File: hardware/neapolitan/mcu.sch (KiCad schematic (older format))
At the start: 134 parts, among them J1 USB-MICRO-B, P1 1V8, P20 GPIO, P22 I2S, P23 DBGEN, P24 TRST, P25 LPC_ISP, P26 LPC_JTAG, P28 SD, P29 CPLD_JTAG, P3 GND, P30 BANK2_AUX, P5 LEDS, P68 SPIFI_CS, P69 VREGMODE, P70 EN_1V8, P71 ID, P72 GP_CLKIN, P73 P1_2, P74 P1_1, P75 GP_CLKIN, P76 GP_CLKIN, P77 GP_CLKIN, P78 GP_CLKIN, P79 GP_CLKIN, P8 VCC, P80 SHIELD, P81 SPIFI_SIO2, P82 SPIFI_SIO3, Q5 MOSFET_P, SW1 DFU, SW2 RESET, U15 LXES1TBCC2-004, U20 W25Q80BV, U21 TPS62410, U23 LPC4320FBD144, U24 GSG-XC2C64A-7VQG100C, X2 MCU_XTAL, X3 RTC_XTAL

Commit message: Neapolitan: deleted MCU and other things not needed
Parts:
- removed C118, C157, C158, C164: 18pF, hackrf:GSG-0402, symbol C
- removed C125: 33pF, hackrf:GSG-0402, symbol C
- removed C126, C127, C143, C145, C146: 10uF, hackrf:GSG-0805, symbol C
- removed C128, C129, C130, C131, C132, C133, C134, C135, C136, C137, C138, C139, C140, C141, C142, C144, C147, C148, C149, C150, C151, C152, C153, C154: 100nF, hackrf:GSG-0402, symbol C
- removed C156: 47pF, hackrf:GSG-0402, symbol C
- removed D4: USBLED, gsg-modules:LTST-S220, symbol LED
- removed D8: 1V8LED, gsg-modules:LTST-S220, symbol LED
- removed L10, L11: 4u7, hackrf:GSG-NRG4026, symbol INDUCTOR
- removed P1: 1V8, hackrf:GSG-HEADER-1x2, symbol CONN_2
- removed P23: DBGEN, hackrf:GSG-TESTPOINT-50MIL, symbol CONN_1
- removed P24: TRST, hackrf:GSG-TESTPOINT-50MIL, symbol CONN_1
- removed P25: LPC_ISP, hackrf:GSG-HEADER-1x6, symbol CONN_6
- removed P26: LPC_JTAG, hackrf:GSG-50MIL-HEADER-2x5-TH, symbol CONN_5X2
- removed P29: CPLD_JTAG, hackrf:GSG-HEADER-1x2, symbol CONN_2
- removed P3: GND, hackrf:GSG-HEADER-NOMARK-1x2, symbol CONN_2
- removed P68: SPIFI_CS, hackrf:GSG-TESTPOINT-50MIL, symbol CONN_1
- removed P69: VREGMODE, hackrf:GSG-TESTPOINT-50MIL, symbol CONN_1
- removed P70: EN_1V8, hackrf:GSG-TESTPOINT-50MIL, symbol CONN_1
- removed P71: ID, hackrf:GSG-TESTPOINT-50MIL, symbol CONN_1
- removed P72, P75, P76, P77, P78, P79: GP_CLKIN, hackrf:GSG-TESTPOINT-50MIL, symbol CONN_1
- removed P73: P1_2, hackrf:GSG-TESTPOINT-50MIL, symbol CONN_1
- removed P74: P1_1, hackrf:GSG-TESTPOINT-50MIL, symbol CONN_1
- removed P8: VCC, hackrf:GSG-HEADER-1x2, symbol CONN_2
- removed P81: SPIFI_SIO2, hackrf:GSG-TESTPOINT-50MIL, symbol CONN_1
- removed P82: SPIFI_SIO3, hackrf:GSG-TESTPOINT-50MIL, symbol CONN_1
- removed Q5: MOSFET_P, gsg-modules:SOT23GDS, symbol MOSFET_P
- removed R100, R19, R30, R34, R77, R78, R79, R80, R81, R86, R87, R88, R89, R90, R91, R96, R98, R99: 39, hackrf:GSG-0402, symbol R
- removed R12, R37, R48, R49, R51, R52, R54, R59, R63, R64, R65, R66, R67, R68, R7, R93: 10k, hackrf:GSG-0402, symbol R
- removed R46, R55: 162k, hackrf:GSG-0402, symbol R
- removed R47: 330k, hackrf:GSG-0402, symbol R
- removed R56: 715k, hackrf:GSG-0402, symbol R
- removed R57, R58, R62: 0, hackrf:GSG-0402, symbol R
- removed R69: 12k, hackrf:GSG-0402, symbol R
- removed R72: 470, hackrf:GSG-0402, symbol R
- removed R76: 1k, hackrf:GSG-0402, symbol R
- removed SW1: DFU, hackrf:GSG-SWITCH-FSMRA, symbol SW_PUSH_SHIELDED
- removed SW2: RESET, hackrf:GSG-SWITCH-FSMRA, symbol SW_PUSH_SHIELDED
- removed U15: LXES1TBCC2-004, hackrf:GSG-LXES1TBCC2-004, symbol LXES1TBCC2-004
- removed U20: W25Q80BV, hackrf:GSG-SOIC8-208, symbol W25Q80BV
- removed U21: TPS62410, hackrf:GSG-S-PVSON-N10, symbol TPS62410
- removed U23: LPC4320FBD144, hackrf:GSG-LQFP144, symbol LPC43XXFBD144
- removed U24: GSG-XC2C64A-7VQG100C, hackrf:GSG-VQ100, symbol GSG-XC2C64A-7VQG100C
- removed X2: MCU_XTAL, hackrf:GSG-XTAL3.2x2.5mm, symbol GSG-XTAL4PIN
- removed X3: RTC_XTAL, hackrf:GSG-XTAL-AB26TRQ, symbol CRYSTAL
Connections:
- net labels removed: 1V8, BANK2F3M1, BANK2F3M10, BANK2F3M11, BANK2F3M14, BANK2F3M15, BANK2F3M16, BANK2F3M3, BANK2F3M5, BANK2F3M7, BANK2F3M8, BANK2F3M9, CPLD_TDO, CPLD_TMS, CS_AD, DA0, DA1, DA2, DA3, DA4, DA5, DA6, DA7, DBGEN, DD0, DD1, DD2, DD3, DD4, DD5, DD6, DD7, DD8, DD9, DM, DP, EN1V8, GP_CLKIN, ISP, MCU_CLK, P1_1, P1_2, REG_OUT1, REG_OUT2, RREF, RTCX1, RTCX2, SGPIO0, SGPIO1, SGPIO10, SGPIO11, SGPIO12, SGPIO13, SGPIO14, SGPIO15, SGPIO2, SGPIO3, SGPIO4, SGPIO5, SGPIO6, SGPIO7, SGPIO8, SGPIO9, SGPIO_CLK, SPIFI_CS, SPIFI_SIO2, SPIFI_SIO3, TCK, TDI, TDO, TMS, VREGMODE, XTAL1, XTAL2
- wire segments 566 -> 152
- no-connect marks 17 -> 3
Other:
- note removed: "1%"
- note removed: "Boot selection:"
- note removed: "Cortex Debug\nConnector\n(10 pin 50 mil)"
- note removed: "Default boot configuration is SPIFI.\nPress SW1 during reset to switch to\nUSB0 (DFU mode)."
- note removed: "GND"
- note removed: "P1_1"
- note removed: "P1_2"
- note removed: "P2_8"
- note removed: "P2_9"
- note removed: "PCB trace jumper"
- note removed: "SPIFI"
- note removed: "SSP0"
- note removed: "Series resistors are here because of a possible\novershoot/undershoot problem. They may be able to be removed\nsafely. Anyway, they probably will minimize damage in the event of\nSGPIO/CPLD misconfiguration."
- note removed: "U23 starts up on this 12 MHz\ncrystal. This makes it possible\nto use USB0 DFU boot mode.\nIt should be possible to switch\nto GP_CLKIN provided by the\nclock generator IC (MCL_CLK)\nif desired."
- note removed: "USART0"
- note removed: "USART3"
- note removed: "USB0"
- note removed: "VCC"

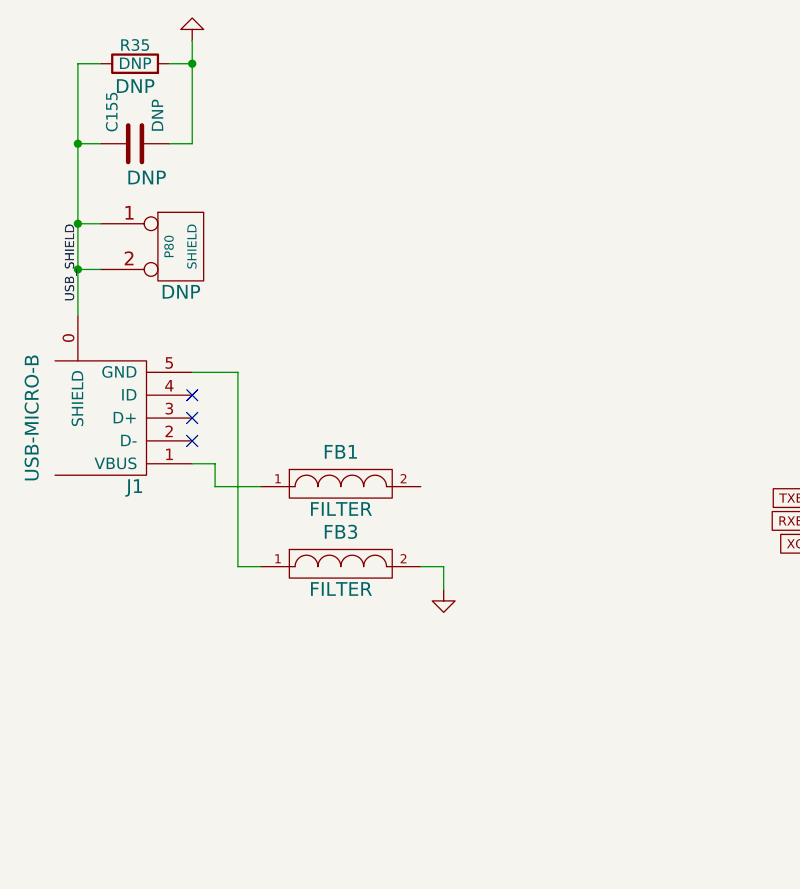
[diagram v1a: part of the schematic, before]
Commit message: Neapolitan: barrel jack and USB power sources that override USB power on main board
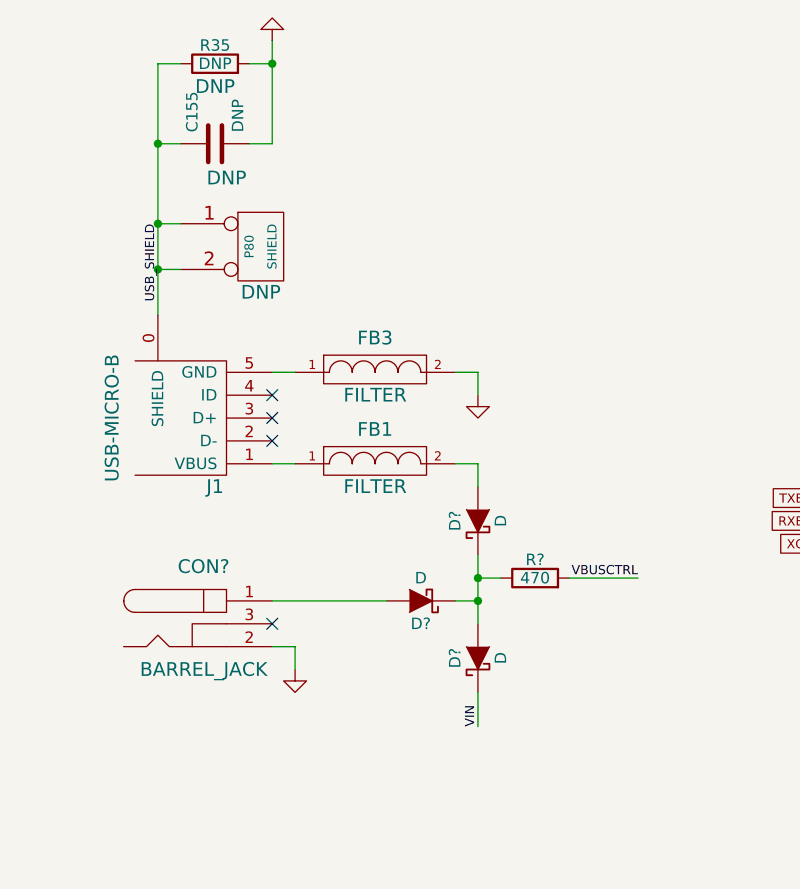
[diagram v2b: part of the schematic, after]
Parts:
- added CON?: BARREL_JACK, symbol BARREL_JACK
- added D? (x3): D, symbol D_Schottky
- added R?: 470, hackrf:GSG-0402, symbol R
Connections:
- wire segments 152 -> 158
- no-connect marks 3 -> 4
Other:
- moved on the sheet: C155, FB1, FB3, J1, P80, R35

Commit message: Neapolitan: header pin assignments
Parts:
- removed P30: BANK2_AUX, hackrf:GSG-HEADER-2x10, symbol CONN_10X2
- D10: renamed from D?; value D -> VIN_DIODE
- D4: renamed from D?; value D -> BARREL_DIODE
- D8: renamed from D?; value D -> VBUS_DIODE
- gave numbers to parts that had none: 2
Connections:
- net labels added: SSP0_MISO, SSP0_MOSI, SSP0_SCK
- net labels removed: B1AUX13, B1AUX14, B2AUX1, B2AUX10, B2AUX11, B2AUX12, B2AUX13, B2AUX14, B2AUX15, B2AUX16, B2AUX2, B2AUX3, B2AUX4, B2AUX5, B2AUX6, B2AUX7, B2AUX8, B2AUX9, BANK2F3M12, BANK2F3M2, BANK2F3M4, BANK2F3M6, CPLD_TCK, CPLD_TDI, GCK0, LED1, SSP1_MISO, SSP1_MOSI, SSP1_SCK
- wire segments 158 -> 116
- no-connect marks 4 -> 13
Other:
- moved on the sheet: D4

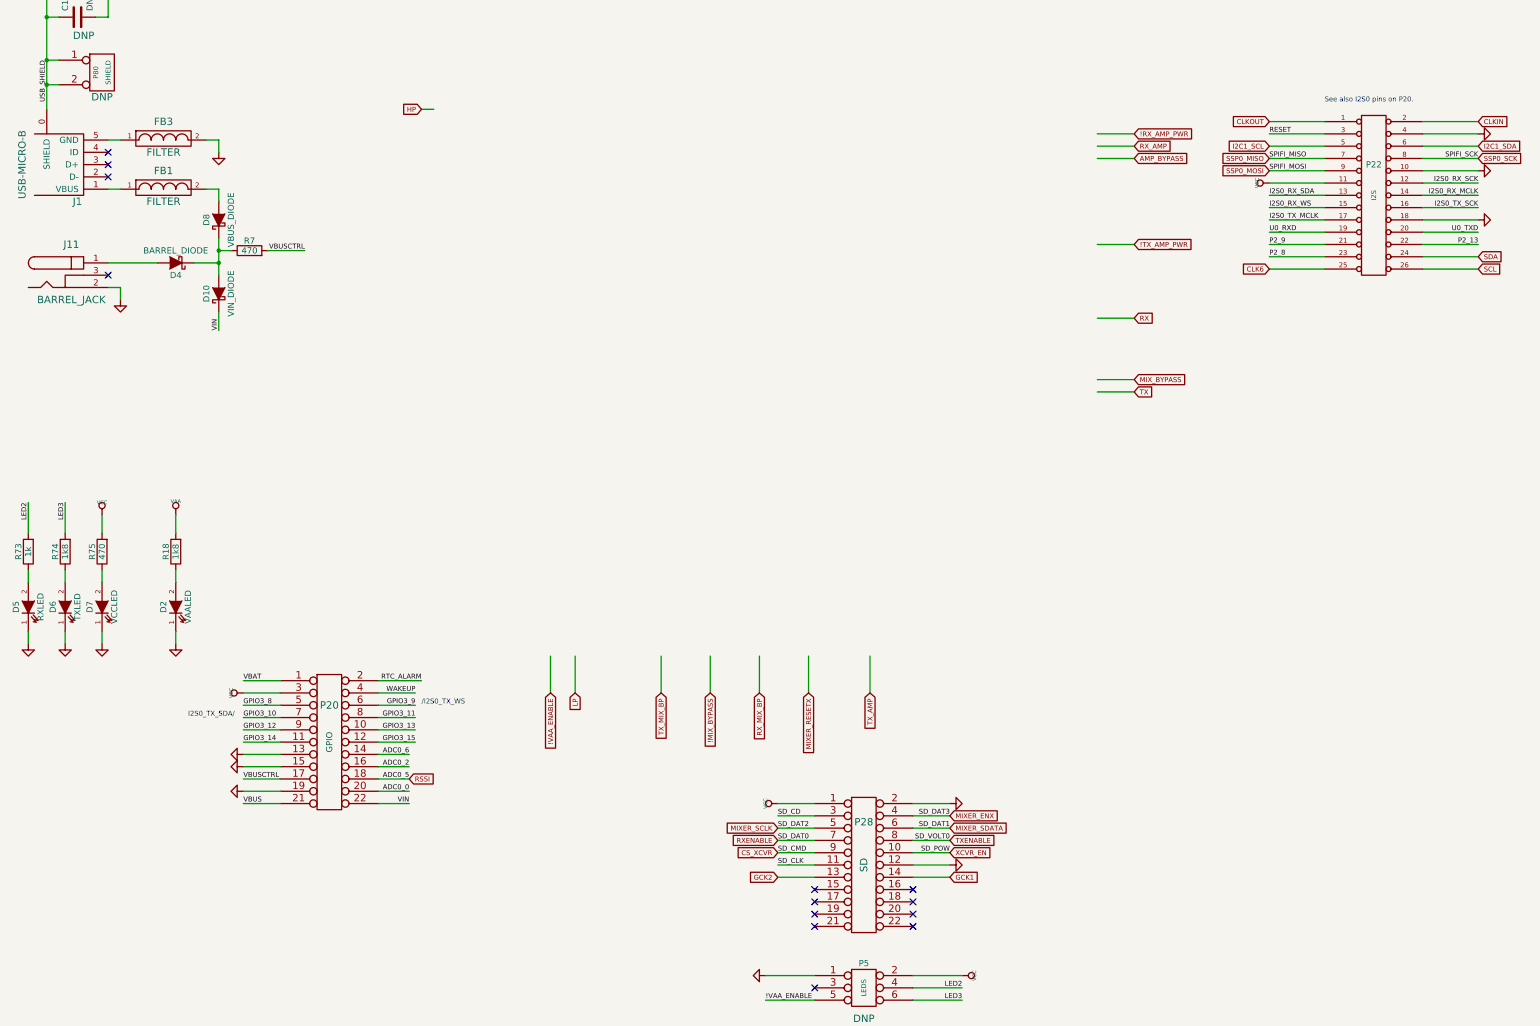
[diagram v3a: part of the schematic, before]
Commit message: Neapolitan: added I/O expander
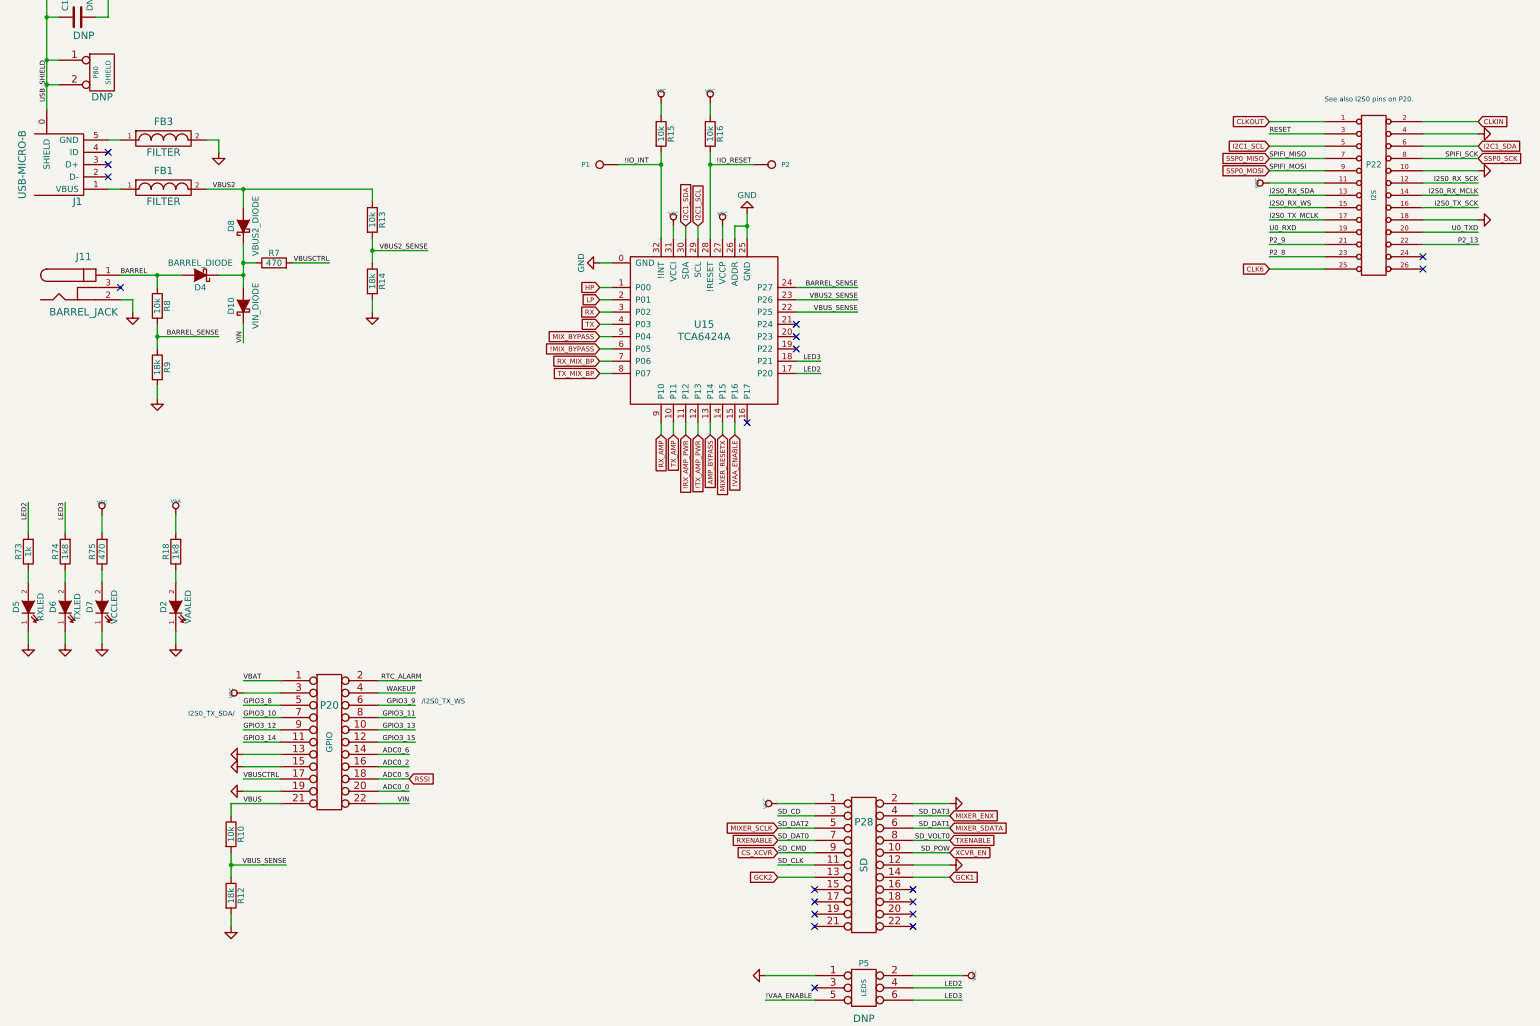
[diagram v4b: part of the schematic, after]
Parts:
- added P1: !IO_INT, hackrf:GSG-TESTPOINT-50MIL, symbol CONN_1
- added P2: !IO_RESET, hackrf:GSG-TESTPOINT-50MIL, symbol CONN_1
- added R10, R13, R15, R16, R8: 10k, hackrf:GSG-0402, symbol R
- added R12, R14, R9: 18k, hackrf:GSG-0402, symbol R
- added U15: TCA6424A, gsg-modules:QFN32-5, symbol TCA6424A
- D10, D4: footprint (none) -> gsg-modules:SOD128
- D8: value VBUS_DIODE -> VBUS2_DIODE; footprint (none) -> gsg-modules:SOD128
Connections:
- net labels added: !IO_INT, !IO_RESET, BARREL, BARREL_SENSE, VBUS2, VBUS2_SENSE, VBUS_SENSE
- net labels removed: SCL, SDA
- wire segments 116 -> 145
- no-connect marks 13 -> 19
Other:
- moved on the sheet: D10, D4, D8, J11, R7

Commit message: Neapolitan: barrel jack module
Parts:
- J11: footprint (none) -> gsg-modules:CUI_PJ-102[AB]H
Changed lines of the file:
@@
 F 0 "J11" H 1450 4700 60  0000 C CNN
 F 1 "BARREL_JACK" H 1450 4250 60  0000 C CNN
-F 2 "" H 1450 4450 60  0001 C CNN
+F 2 "gsg-modules:CUI_PJ-102[AB]H" H 1450 4450 60  0001 C CNN
 F 3 "" H 1450 4450 60  0000 C CNN
 F 4 "CUI" H 1450 4450 60  0001 C CNN "Manufacturer"

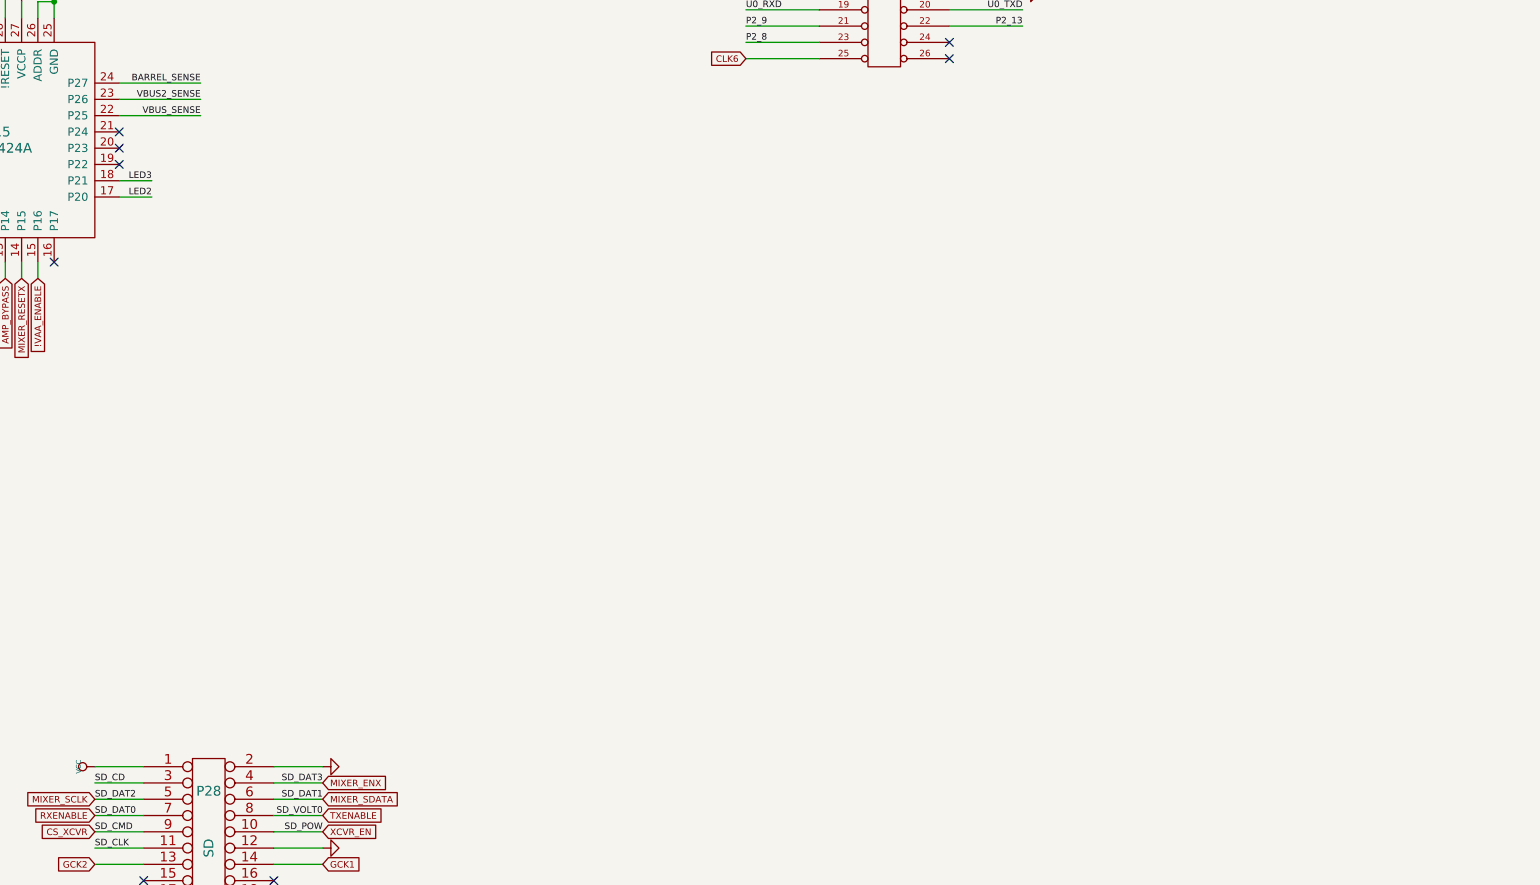
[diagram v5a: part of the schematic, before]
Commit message: Neapolitan: experimental 2.5 ppm clock in schematic
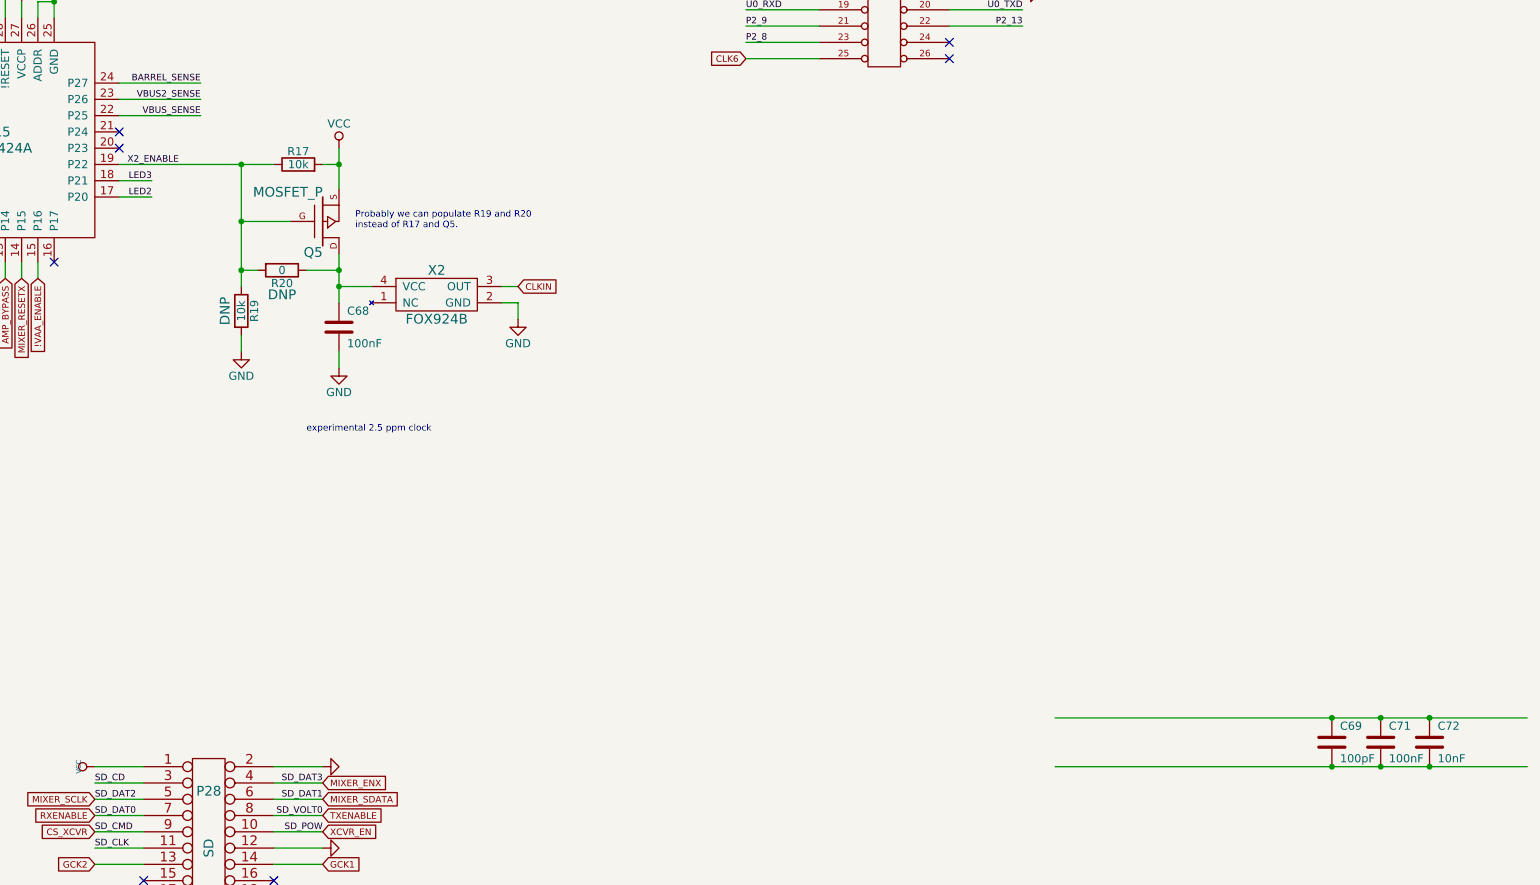
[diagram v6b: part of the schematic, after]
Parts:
- added C68, C71: 100nF, hackrf:GSG-0402, symbol C
- added C69: 100pF, hackrf:GSG-0402, symbol C
- added C72: 10nF, hackrf:GSG-0402, symbol C
- added Q5: MOSFET_P, gsg-modules:SOT23GDS, symbol MOSFET_P
- added R17, R19: 10k, hackrf:GSG-0402, symbol R
- added R20: 0, hackrf:GSG-0402, symbol R
- added X2: FOX924B, symbol FOX924B
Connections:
- net CLKIN: now also X2.3 (OUT)
- net GND: now also C68.2, R19.2, X2.2 (GND)
- net VCC: now also Q5.S, R17.2
- net X2_ENABLE: now reaches U15.19 (P22)
- net X2_ENABLE: now also Q5.G, R17.1, R19.1, R20.2
- new net: C68.1, Q5.D, R20.1, X2.4 (VCC)
- new net: C69.1, C71.1, C72.1
- new net: C69.2, C71.2, C72.2
- no-connect marks 19 -> 18
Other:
- note added: "Probably we can populate R19 and R20\ninstead of R17 and Q5."
- note added: "experimental 2.5 ppm clock"
